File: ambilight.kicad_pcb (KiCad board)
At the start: 2 copper layers, 43 x 21.5 mm, 34 parts, among them J1 TYPE-C-31-M-12, J2 RGB Connector, J3 Power Connector, U1 AZ1117CR-3.3TRG1, U2 ESP32-C3-MINI-1-H4, U3 MCP1416, U4 USBLC6-2SC6

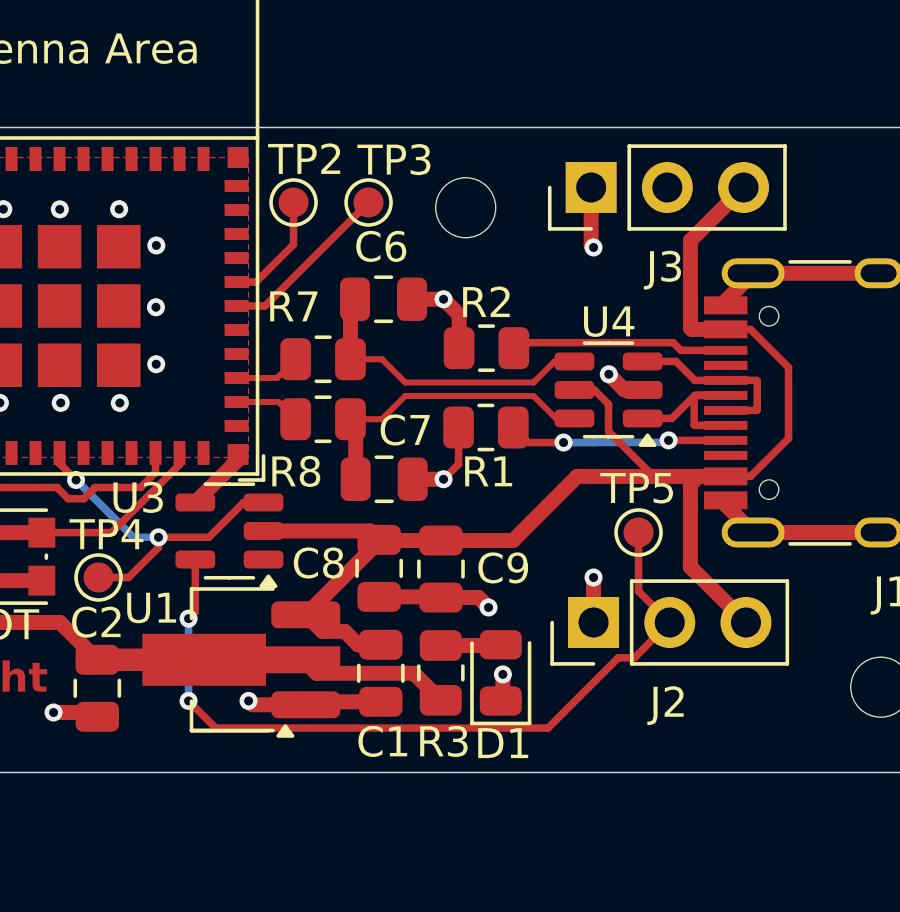
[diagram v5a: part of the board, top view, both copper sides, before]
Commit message: Fix resistor values
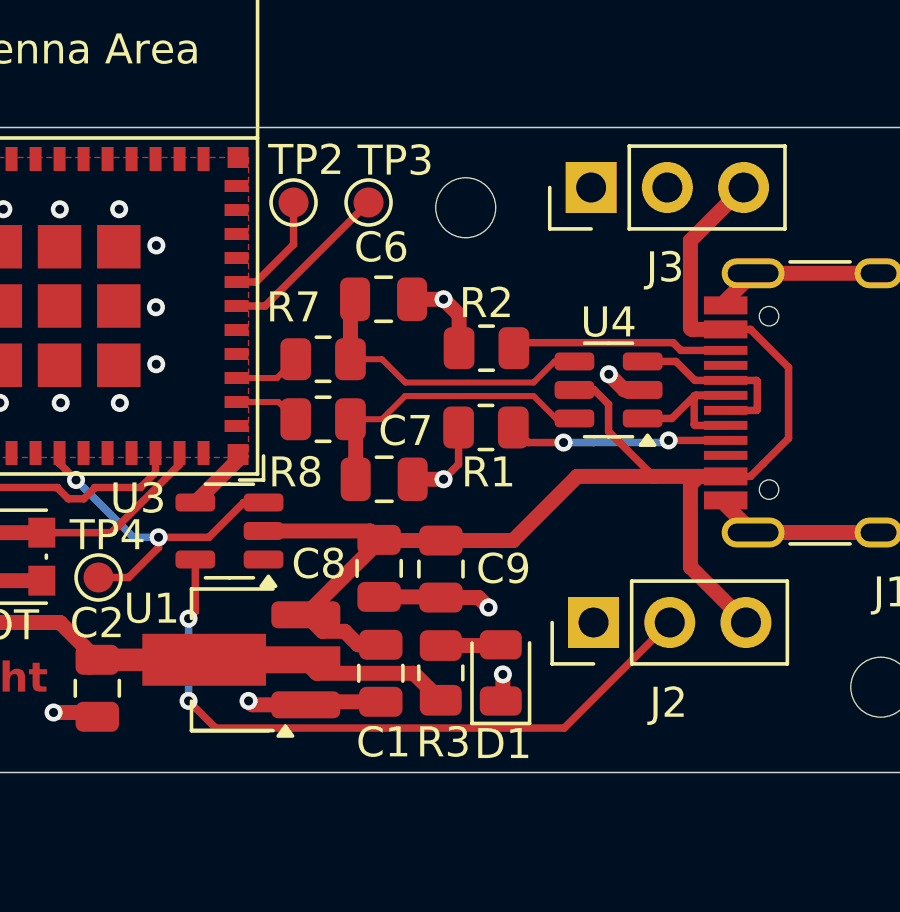
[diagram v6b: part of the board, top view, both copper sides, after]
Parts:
- removed TP5: ~, Custom_PCBWay:TestPoint_Pad_D1.0mm_SilkscreenFix
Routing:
- net GND: track 47.9 -> 44.4 mm, vias 26 -> 24
- net Net-(J2-Pin_2): track 26.1 -> 22.7 mm
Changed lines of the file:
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@@
-		(embedded_fonts no)
-	)
-	(footprint "Custom_PCBWay:TestPoint_Pad_D1.0mm_SilkscreenFix"
-		(layer "F.Cu")
-		(at 90.5 42.5)
-		(descr "SMD pad as test Point, diameter 1.0mm")
-		(tags "test point SMD pad")
-		(property "Reference" "TP5"
-			(at 0 -1.448 0)
-			(layer "F.SilkS")
-			(effects
-				(font
-					(size 1 1)
-					(thickness 0.15)
-				)
-			)
-		)
-		(property "Value" "~"
-			(at 0 1.55 0)
-			(layer "F.Fab")
-			(effects
-				(font
-					(size 1 1)
-					(thickness 0.15)
-				)
-			)
-		)
-		(property "Datasheet" ""
-			(at 0 0 0)
-			(unlocked yes)
-			(layer "F.Fab")
-			(hide yes)
-			(effects
-				(font
-					(size 1.27 1.27)
-					(thickness 0.15)
-				)
-			)
-		)
-		(property "Description" "test point"
-			(at 0 0 0)
-			(unlocked yes)
-			(layer "F.Fab")
-			(hide yes)
-			(effects
-				(font
-					(size 1.27 1.27)
-					(thickness 0.15)
-				)
-			)
-		)
-		(property ki_fp_filters "Pin* Test*")
-		(sheetname "/")
-		(sheetfile "ambilight.kicad_sch")
-		(attr exclude_from_pos_files)
-		(fp_circle
-			(center 0 0)
-			(end 0.75 0)
-			(stroke
-				(width 0.12)
-				(type solid)
-			)
-			(fill no)
-			(layer "F.SilkS")
-		)
-		(fp_circle
-			(center 0 0)
-			(end 1 0)
-			(stroke
-				(width 0.05)
-				(type solid)
-			)
-			(fill no)
-			(layer "F.CrtYd")
-		)
-		(fp_text user "${REFERENCE}"
-			(at 0 -1.45 0)
-			(layer "F.Fab")
-			(effects
-				(font
-					(size 1 1)
-					(thickness 0.15)
-				)
-			)
-		)
-		(pad "1" smd circle
-			(at 0 0)
-			(size 1 1)
-			(layers "F.Cu" "F.Mask")
-			(net 8 "Net-(J2-Pin_2)")
-			(pinfunction "1")
-			(pintype "passive")
-		)
 		(embedded_fonts no)
 	)
@@
 	)
 	(segment
-		(start 89.824 46.676)
-		(end 90.364 46.676)
+		(start 88.021147 49.018853)
+		(end 91.54 45.5)
 		(width 0.25)
 		(layer "F.Cu")
@@
 	)
 	(segment
-		(start 76.4045 49.018853)
-		(end 87.481147 49.018853)
+		(start 75.5 48.114353)
+		(end 76.4045 49.018853)
 		(width 0.25)
 		(layer "F.Cu")
@@
 	)
 	(segment
-		(start 75.5 48.114353)
-		(end 76.4045 49.018853)
-		(width 0.25)
-		(layer "F.Cu")
-		(net 8)
-	)
-	(segment
 		(start 75.725 43.4)
 		(end 75.725 45.146353)
@@
 	)
 	(segment
-		(start 91.54 45.5)
-		(end 90.5 44.46)
-		(width 0.25)
-		(layer "F.Cu")
-		(net 8)
-	)
-	(segment
-		(start 90.5 44.46)
-		(end 90.5 42.5)
-		(width 0.25)
-		(layer "F.Cu")
-		(net 8)
-	)
-	(segment
-		(start 90.364 46.676)
-		(end 91.54 45.5)
-		(width 0.25)
-		(layer "F.Cu")
-		(net 8)
-	)
-	(segment
-		(start 87.481147 49.018853)
-		(end 89.824 46.676)
+		(start 76.4045 49.018853)
+		(end 88.021147 49.018853)
 		(width 0.25)
 		(layer "F.Cu")
@@
 	)
 	(segment
-		(start 88.92 31)
-		(end 88.92 32.92)
-		(width 0.5)
-		(layer "F.Cu")
-		(net 18)
-	)
-	(segment
 		(start 83.891407 44.646198)
 		(end 83.91321 44.668001)
@@
 	)
 	(segment
-		(start 88.92 32.92)
-		(end 89 33)
-		(width 0.5)
-		(layer "F.Cu")
-		(net 18)
-	)
-	(segment
 		(start 61.5 38.5)
 		(end 60.5 39.5)
@@
 	)
 	(segment
-		(start 89 45.5)
-		(end 89 44)
-		(width 0.5)
-		(layer "F.Cu")
-		(net 18)
-	)
-	(segment
 		(start 79.407709 48.242853)
 		(end 77.6285 48.242853)
@@
 	)
 	(via
-		(at 89 33)
-		(size 0.6)
-		(drill 0.3)
-		(layers "F.Cu" "B.Cu")
-		(free yes)
-		(net 18)
-	)
-	(via
 		(at 69.210193 38.179565)
 		(size 0.6)
@@
 		(size 0.6)
 		(drill 0.3)
-		(layers "F.Cu" "B.Cu")
-		(free yes)
-		(net 18)
-	)
-	(via
-		(at 89 44)
-		(size 0.6)
-		(drill 0.3)

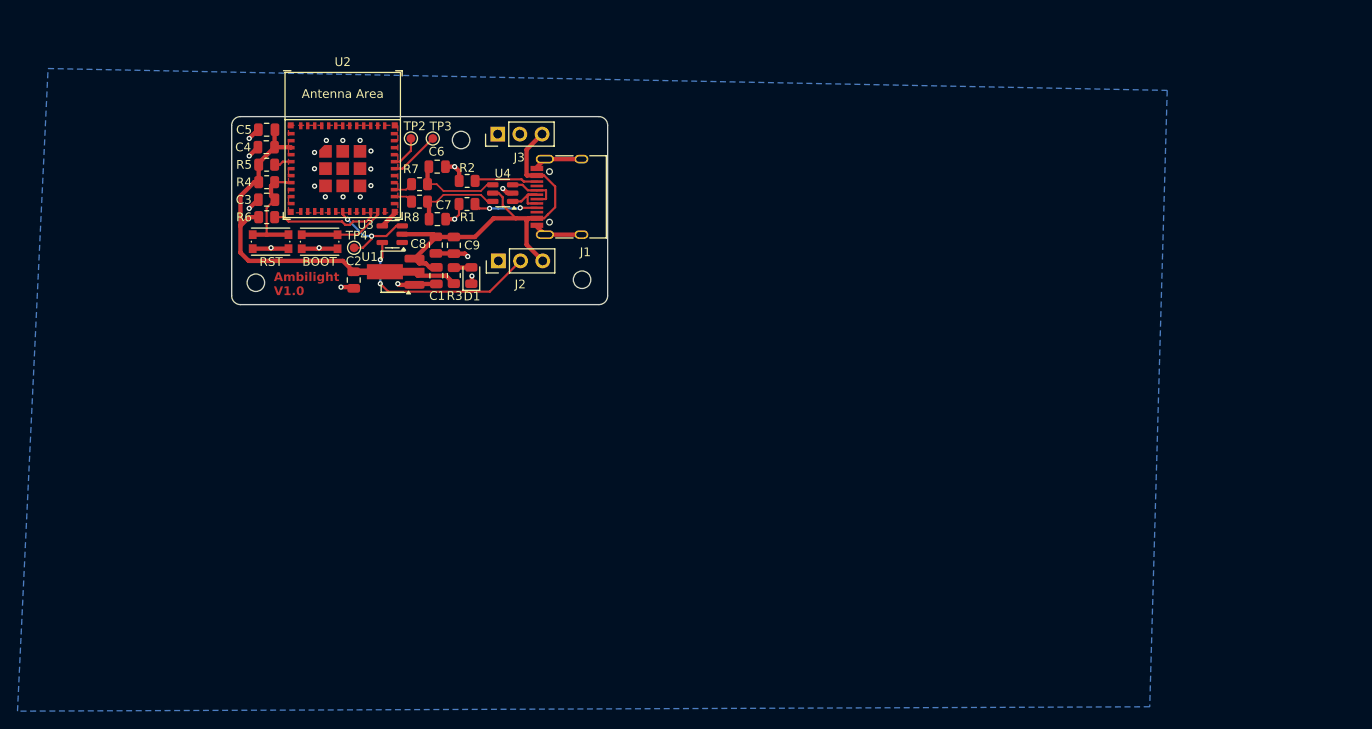
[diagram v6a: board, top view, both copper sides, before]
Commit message: Many small-ish changes, generate production files
Some components were changed to get better deal at manufacturer. The
files in the production folder are the ones sent to the manufacturer for
this release.
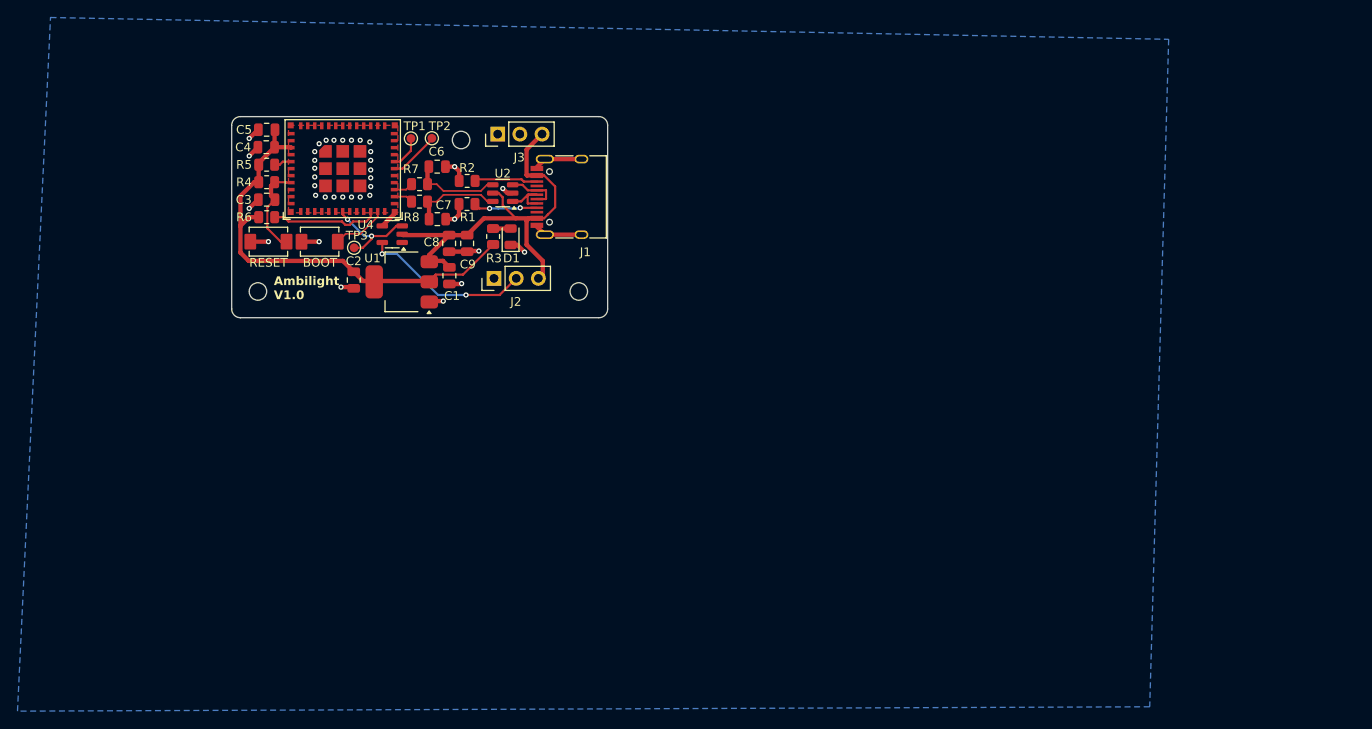
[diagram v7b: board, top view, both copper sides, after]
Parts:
- removed RST: RESET, Button_Switch_SMD:SW_Push_1P1T_NO_CK_KMR2
- added SW1: RESET, Button_Switch_additional:TS-1088-AR02016, F.Cu at (62.7, 43.3)
- C3: value 0.1uF -> 1uF
- R1, R2: value 5.1kR -> 5.1k
- R3: value 120R -> 330R
- R4, R5, R6: value 10kR -> 10k
- SW2: renamed from BOOT; footprint Button_Switch_SMD:SW_Push_1P1T_NO_CK_KMR2 -> Button_Switch_additional:TS-1088-AR02016
- U1: value AZ1117CR-3.3TRG1 -> AZ1117CH-3.3TRG1; footprint Package_TO_SOT_SMD:SOT-89-3_Handsoldering -> Package_TO_SOT_SMD:SOT-223-3_TabPin2
- moved REF** 37.1 mm to (61.5, 49.0)
- moved REF** 36.9 mm to (98.2, 49.0)
- moved R3 6.34 mm to (88.4, 42.7)
- moved D1 6.32 mm to (90.4, 42.7)
- moved J2 2.06 mm to (88.5, 47.5)
- moved C9 1.53 mm to (85.4, 43.5)
- moved C8 1.53 mm to (83.4, 43.5)
- moved U1 1.52 mm to (78.0, 47.9)
- moved C1 1.49 mm to (83.4, 47.2)
- moved TP2 0.11 mm to (81.4, 31.5)
- turned SW2 to 90 degrees
- renumbered TP2 to TP1, TP3 to TP2, TP4 to TP3, U4 to U2, U2 to U3, U3 to U4
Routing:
- net +3V3: track 46.6 -> 52.7 mm
- net GND: track 44.4 -> 38.7 mm, vias 24 -> 37
- net Net-(U3-GPIO9): track 10.0 -> 6.35 mm
- net Net-(J2-Pin_2): track 22.7 -> 19.4 mm
- net VCC: track 47.2 -> 49.3 mm
- net Net-(U3-EN/CHIP_PU): track 13.1 -> 11.1 mm
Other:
- board size 43 x 21.5 mm -> 43 x 23 mm
